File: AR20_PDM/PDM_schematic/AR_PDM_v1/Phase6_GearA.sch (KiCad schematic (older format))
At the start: 22 parts, among them Q1 BTS50025-1TAD, U1 INA233

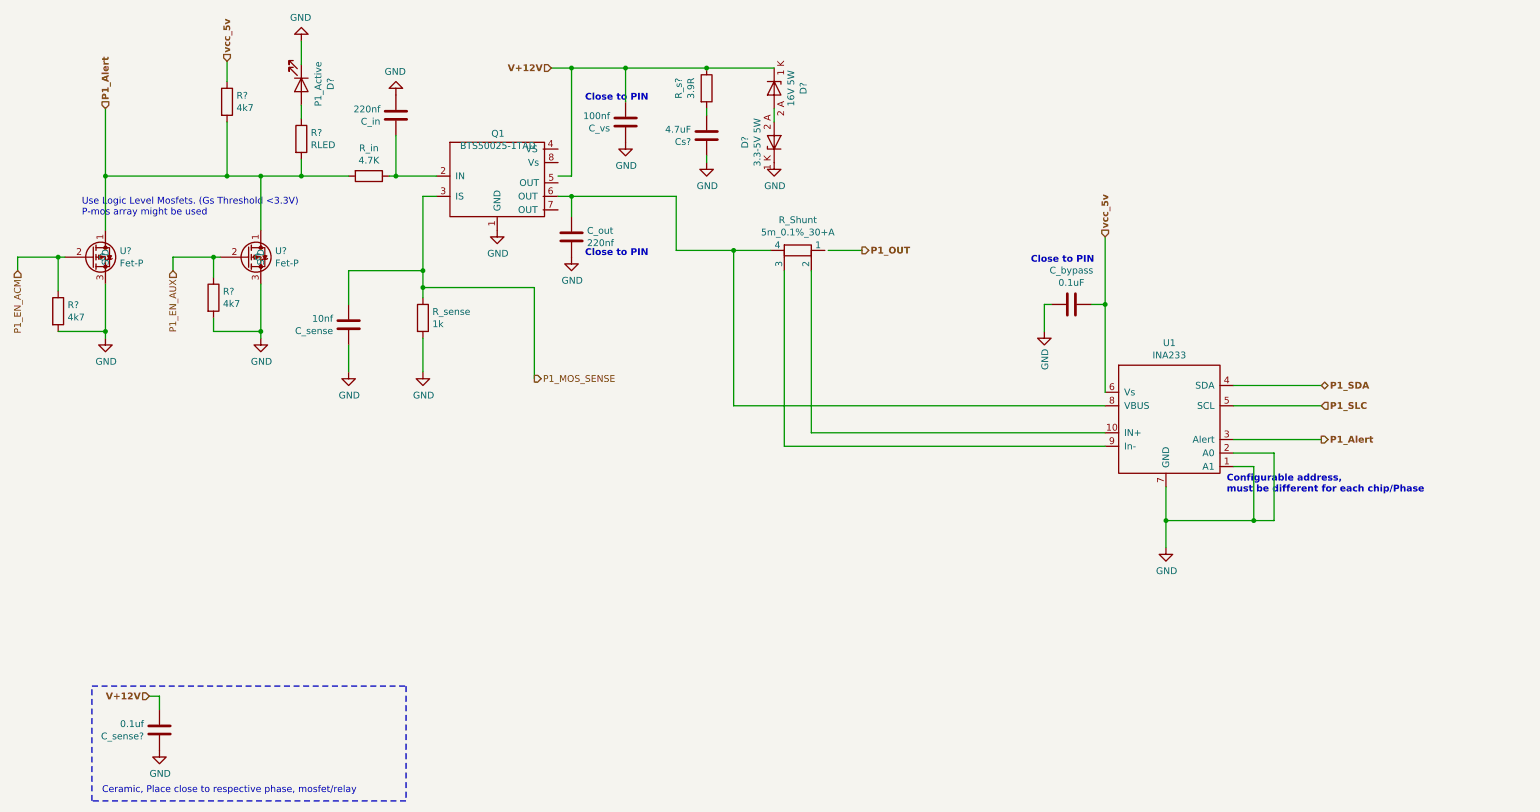
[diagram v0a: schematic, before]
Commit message: Major Schematics changes-work in progress
- Added rest of the phases
- Corrected pin names, and began to connect everything
- Began mapping the connectors, Pin-out not yet verified for all connectors
- Began mapping of user interface (Led indicators)
- INA233 now senses OUT voltage on mosfets instead of main 12Volt
- Added extra decoupling capacitors
Known things to fix:
- AUX inputs activation method, and a disconnect switch on phase 1-7 (mosfets)
- Rest of the user interface
- Find correct plugs for the system
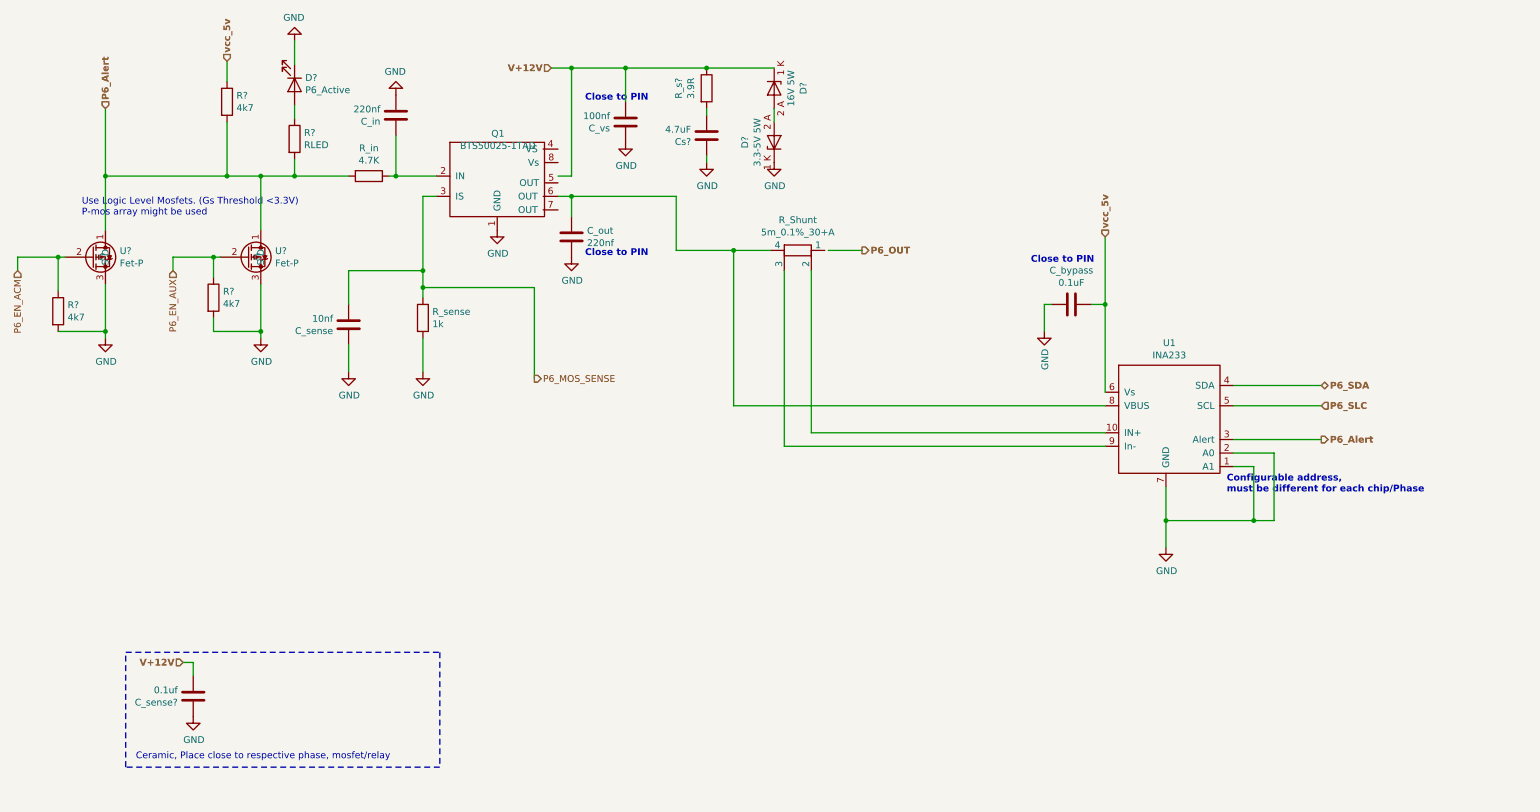
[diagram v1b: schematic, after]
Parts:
- removed C_sense?: 0.1uf, symbol AR20_PDM_v1-rescue:C-Device
- removed D?: P1_Active, symbol Device:LED
- removed R?: RLED, symbol AR20_PDM_v1-rescue:R-Device
- added C_sense?: 0.1uf, symbol AR20_PDM_v1-rescue:C-Device
- added D?: P6_Active, symbol Device:LED
- added R?: RLED, symbol AR20_PDM_v1-rescue:R-Device
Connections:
- net GND: now also C_sense?.1, D?.1 (K)
- net V+12V: now also C_sense?.2
- net P1_Alert renamed P6_Alert
- net P6_Alert: now also R?.2
- net P1_EN_ACM renamed P6_EN_ACM
- net P1_EN_AUX renamed P6_EN_AUX
- net P1_MOS_SENSE renamed P6_MOS_SENSE
- net P1_SDA renamed P6_SDA
- net P1_SLC renamed P6_SLC
- new net: D?.2 (A), R?.1

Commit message: Added LEDs and switches.
- Added all status leds
- Added all switches
- ! Connections are work in progress, not everything is correct
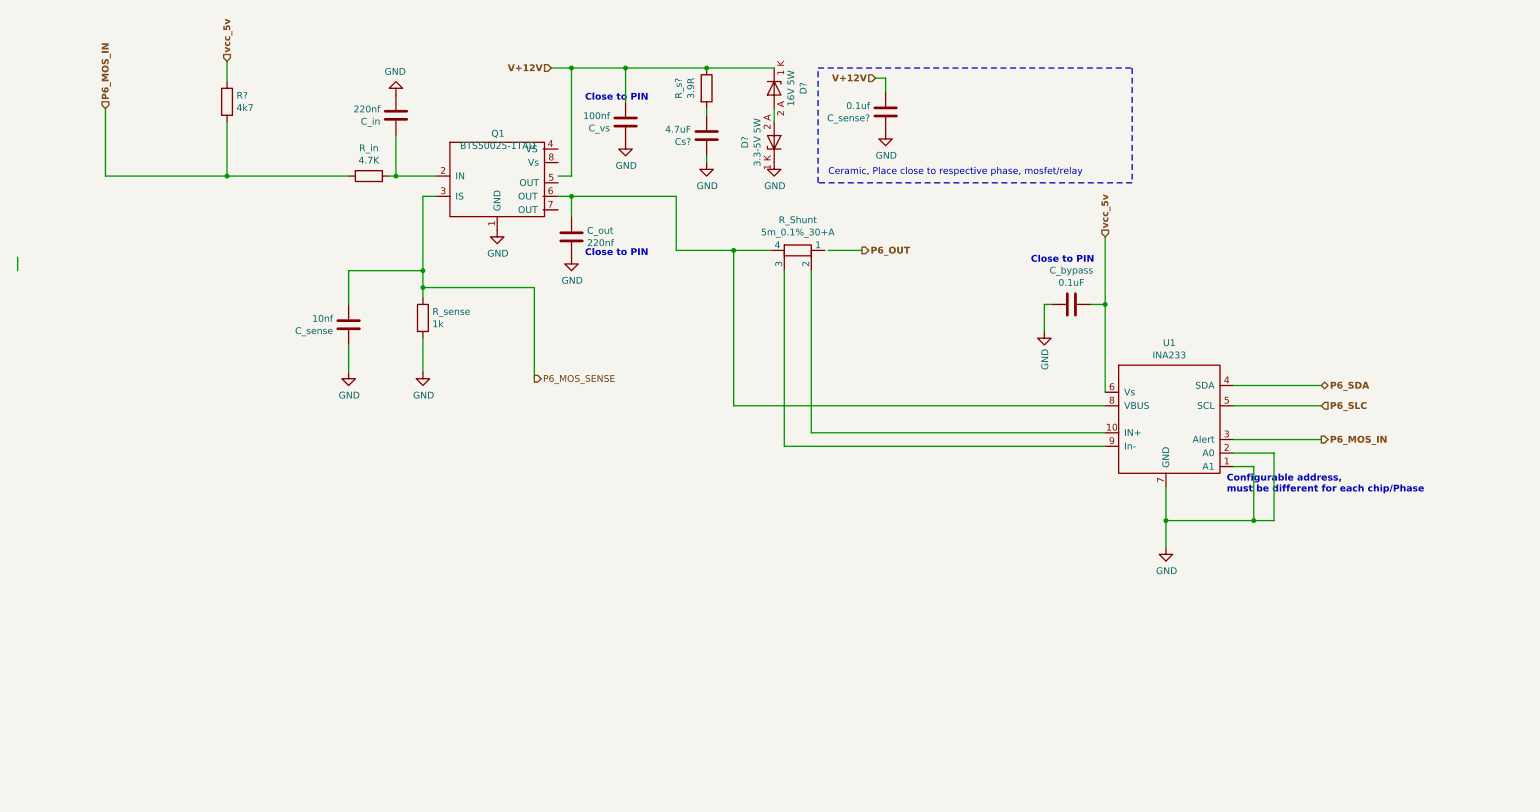
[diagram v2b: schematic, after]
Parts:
- removed D?: P6_Active, symbol Device:LED
- removed R? (x2): 4k7, symbol AR20_PDM_v1-rescue:R-Device
- removed R?: RLED, symbol AR20_PDM_v1-rescue:R-Device
- removed U? (x2): Fet-P, symbol AR20_PDM_v1-rescue:GenericFet-P
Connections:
- net labels added: P6_MOS_IN
- net labels removed: P6_Alert, P6_EN_ACM, P6_EN_AUX
- wire segments 81 -> 60
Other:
- note removed: "Use Logic Level Mosfets. (Gs Threshold <3.3V)\nP-mos array might be used"
- moved on the sheet: C_sense?

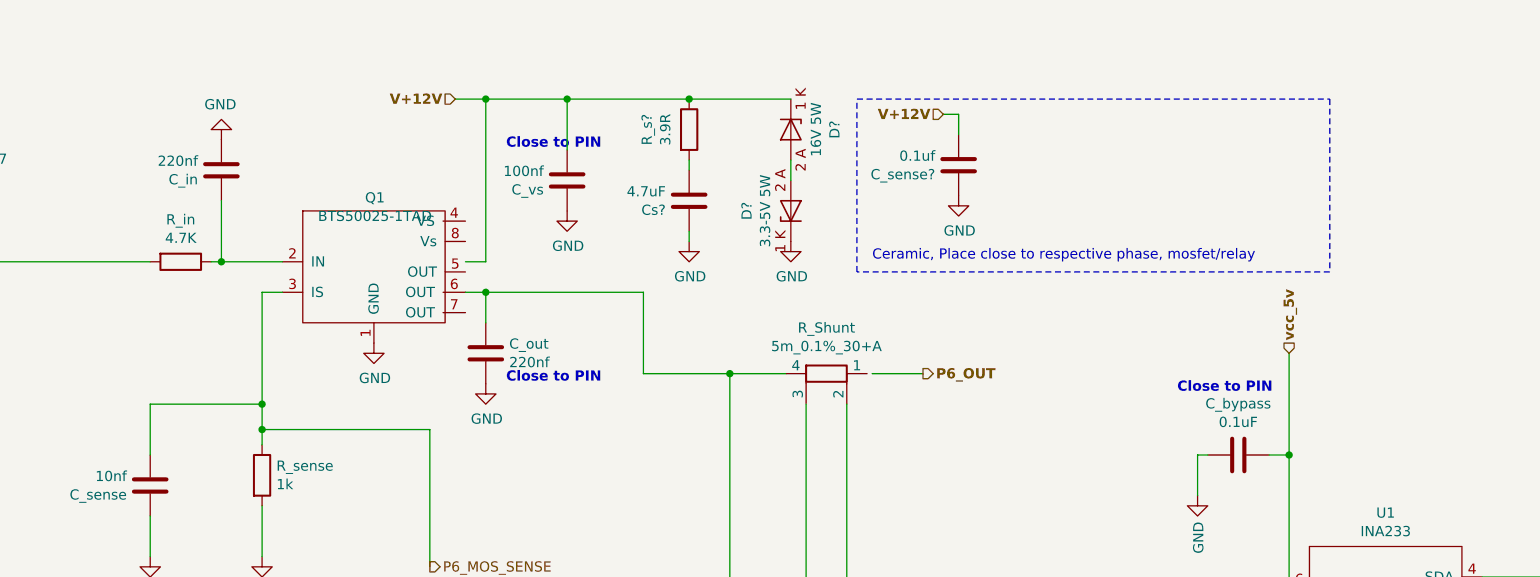
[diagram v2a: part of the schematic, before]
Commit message: Fixed wrong value components and ports, wiring, see discription
- Fixed supply cappacitor value 220 nf to 100nf
- Fixed IN cappacitor value 220 nf to 150 nf
- Fixed out cappacitor value, 220nf to 10 nf
- Made a mux for mosfet sense
- Found a I/O port expander
- Added some and removed some leds
- Fixed all labels, and wired everything up, besides the connectors
- Still missing connector and acm connector pinout.
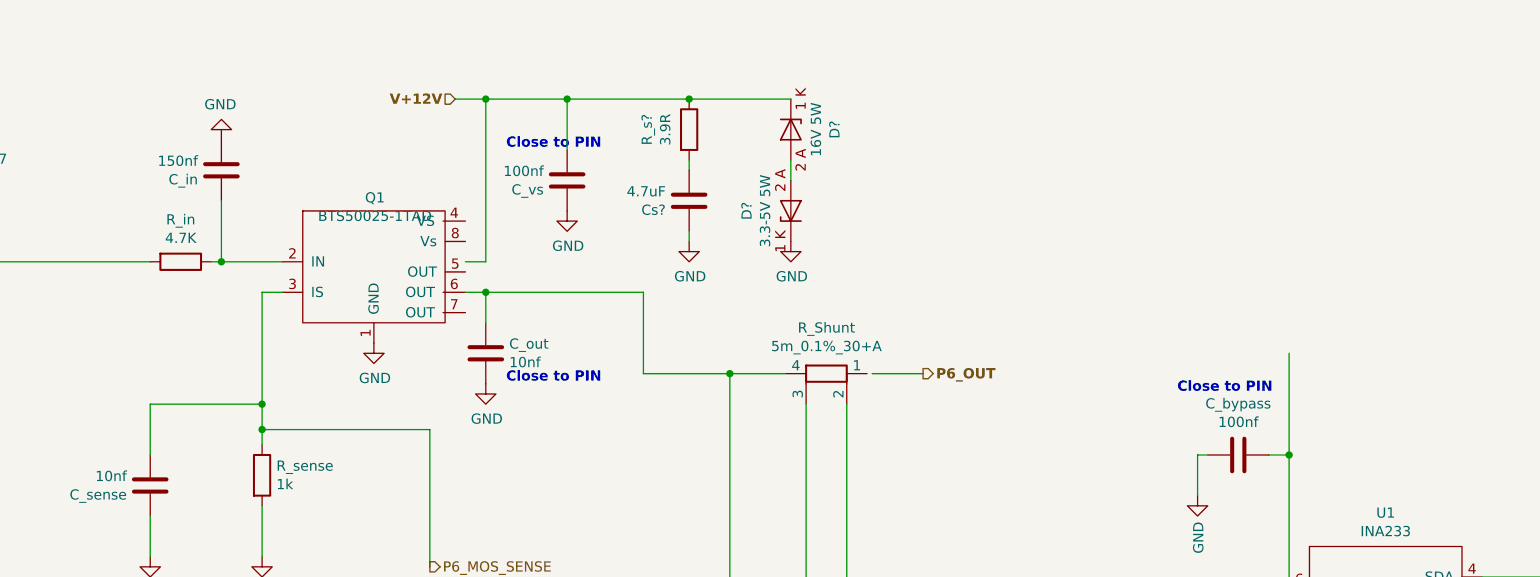
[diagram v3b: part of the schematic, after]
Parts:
- removed C_sense?: 0.1uf, symbol AR20_PDM_v1-rescue:C-Device
- C_bypass: value 0.1uF -> 100nf
- C_in: value 220nf -> 150nf
- C_out: value 220nf -> 10nf
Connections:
- wire segments 60 -> 58
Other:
- note removed: "Ceramic, Place close to respective phase, mosfet/relay"
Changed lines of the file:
@@
 $Descr A4 11693 8268
 encoding utf-8
-Sheet 7 11
+Sheet 7 13
 Title ""
 Date ""
@@
 AR Path="/5E10174B/5DAAC1D1" Ref="C_out?"  Part="1"
 F 0 "C_out?" H 4915 2896 50  0000 L CNN
-F 1 "220nf" H 4915 2805 50  0000 L CNN
+F 1 "10nf" H 4915 2805 50  0000 L CNN
 F 2 "" H 4838 2700 50  0001 C CNN
 F 3 "~" H 4800 2850 50  0001 C CNN
@@
 AR Path="/5E10174B/5DAAC1D7" Ref="C_in?"  Part="1"
 F 0 "C_in?" H 3615 1996 50  0000 L CNN
-F 1 "220nf" H 3615 1905 50  0000 L CNN
+F 1 "150nf" H 3615 1905 50  0000 L CNN
 F 2 "" H 3538 1800 50  0001 C CNN
 F 3 "~" H 3500 1950 50  0001 C CNN
@@
 AR Path="/5E10174B/5DAAC201" Ref="C_bypass?"  Part="1"
 F 0 "C_bypass?" V 8248 3350 50  0000 C CNN
-F 1 "0.1uF" V 8339 3350 50  0000 C CNN
+F 1 "100nf" V 8339 3350 50  0000 C CNN
 F 2 "" H 8538 3200 50  0001 C CNN
 F 3 "~" H 8500 3350 50  0001 C CNN
@@
 	1    0    0    -1
 $EndComp
-Text HLabel 8750 2850 1    50   Input ~ 10
-vcc_5v
 Text HLabel 10350 4350 2    50   Output ~ 10
 P6_MOS_IN
@@
 Text HLabel 4650 1600 0    50   Input ~ 10
 V+12V
-$Comp
-L AR20_PDM_v1-rescue:C-Device C_sense?
-U 1 1 5E1BE4C2
-P 7125 1925
-AR Path="/5DA89415/5E1BE4C2" Ref="C_sense?"  Part="1"
-AR Path="/5DEB10A1/5E1BE4C2" Ref="C_sense?"  Part="1"
-AR Path="/5DEB20EA/5E1BE4C2" Ref="C_sense?"  Part="1"
-AR Path="/5E0E4725/5E1BE4C2" Ref="C_sense?"  Part="1"
-AR Path="/5E0E4A93/5E1BE4C2" Ref="C_sense?"  Part="1"
-AR Path="/5E0E4EB5/5E1BE4C2" Ref="C_sense?"  Part="1"
-AR Path="/5E0E5304/5E1BE4C2" Ref="C_sense?"  Part="1"
-AR Path="/5E0E594B/5E1BE4C2" Ref="C_sense?"  Part="1"
-AR Path="/5E0E607C/5E1BE4C2" Ref="C_sense?"  Part="1"
-AR Path="/5E0FB5C8/5E1BE4C2" Ref="C_sense?"  Part="1"
-AR Path="/5E0FBBBD/5E1BE4C2" Ref="C_sense?"  Part="1"
-AR Path="/5E0FC3A2/5E1BE4C2" Ref="C_sense?"  Part="1"
-AR Path="/5E0FCFDC/5E1BE4C2" Ref="C_sense?"  Part="1"
-AR Path="/5E0FDCCC/5E1BE4C2" Ref="C_sense?"  Part="1"
-AR Path="/5E10174B/5E1BE4C2" Ref="C_sense?"  Part="1"
-F 0 "C_sense?" H 7240 1971 50  0000 L CNN
-F 1 "0.1uf" H 7240 1880 50  0000 L CNN
-F 2 "" H 7163 1775 50  0001 C CNN
-F 3 "~" H 7125 1925 50  0001 C CNN
-	1    7125 1925
-	-1   0    0    1
-$EndComp
-$Comp
-L AR20_PDM_v1-rescue:GND-power #PWR?
-U 1 1 5E1BE4C8
-P 7125 2075
-AR Path="/5DA89415/5E1BE4C8" Ref="#PWR?"  Part="1"
-AR Path="/5DEB10A1/5E1BE4C8" Ref="#PWR?"  Part="1"
-AR Path="/5DEB20EA/5E1BE4C8" Ref="#PWR?"  Part="1"
-AR Path="/5E0E4725/5E1BE4C8" Ref="#PWR?"  Part="1"
-AR Path="/5E0E4A93/5E1BE4C8" Ref="#PWR?"  Part="1"
-AR Path="/5E0E4EB5/5E1BE4C8" Ref="#PWR?"  Part="1"
-AR Path="/5E0E5304/5E1BE4C8" Ref="#PWR?"  Part="1"
-AR Path="/5E0E594B/5E1BE4C8" Ref="#PWR?"  Part="1"
-AR Path="/5E0E607C/5E1BE4C8" Ref="#PWR?"  Part="1"
-AR Path="/5E0FB5C8/5E1BE4C8" Ref="#PWR?"  Part="1"
-AR Path="/5E0FBBBD/5E1BE4C8" Ref="#PWR?"  Part="1"
-AR Path="/5E0FC3A2/5E1BE4C8" Ref="#PWR?"  Part="1"
-AR Path="/5E0FCFDC/5E1BE4C8" Ref="#PWR?"  Part="1"
-AR Path="/5E0FDCCC/5E1BE4C8" Ref="#PWR?"  Part="1"
-AR Path="/5E10174B/5E1BE4C8" Ref="#PWR?"  Part="1"
-F 0 "#PWR?" H 7125 1825 50  0001 C CNN
-F 1 "GND" H 7130 1902 50  0000 C CNN
-F 2 "" H 7125 2075 50  0001 C CNN
-F 3 "" H 7125 2075 50  0001 C CNN
-	1    7125 2075
-	1    0    0    -1
-$EndComp
-Wire Wire Line
-	7125 1775 7125 1675
-Wire Wire Line
-	7125 1675 7050 1675
-Text Notes 6700 2400 0    50   ~ 0
-Ceramic, Place close to respective phase, mosfet/relay
-Text HLabel 7050 1675 0    50   Input ~ 10
-V+12V
-Wire Notes Line
-	6625 1600 8950 1600
-Wire Notes Line
-	8950 1600 8950 2450
-Wire Notes Line
-	8950 2450 6625 2450
-Wire Notes Line
-	6625 2450 6625 1600
 Wire Wire Line
 	2250 2400 3150 2400
